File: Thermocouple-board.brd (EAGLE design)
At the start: 76.2 x 76.2 mm, 78 parts, among them J1 RJ45, J11 1X2-3.5MM, J12 1X2-3.5MM, J13 1X2-3.5MM, J14 1X2-3.5MM, J2 RJ45, J3 1981584-1, J4 2.1MMJACKTHM, J5 ST-LINK, J6 HEADER-1X3, J7 HEADER-1X2, SW1 PUSHBUTTON, SW2 PUSHBUTTON, U1 STM32F042K4, U10 MAX31855, U11 MAX31855, U12 MAX31855, U13 MAX31855, U20 EEPROM-I2C, U21 EEPROM-I2C, U30 ST3485, U31 ST3485, U40 LP298XS, X1 NX3225GD

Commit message: WIP on larger MTG holes
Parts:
- added MH1, MH2, MH3, MH4: 4-40, Thermocouple-board:MTG_HOLE_C280_H125
- added U$3, U$6: MOUNTINGHOLE2.0, microbuilder:MOUNTINGHOLE_2.0_PLATED
- moved J1 3.30 mm to (7.62, 62.7)
- moved J2 3.30 mm to (68.6, 62.7)
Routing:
- net GND: track 588.2 -> 596.4 mm
- net POE_PWR: track 58.5 -> 66.0 mm
- net UP_LINK_B: track 45.4 -> 52.0 mm
- net UP_LINK_A: track 50.6 -> 57.2 mm
- net DN_LINK_B: track 45.1 -> 51.7 mm
- net DN_LINK_A: track 50.2 -> 56.8 mm
- net +3V3: track 393.2 -> 394.7 mm

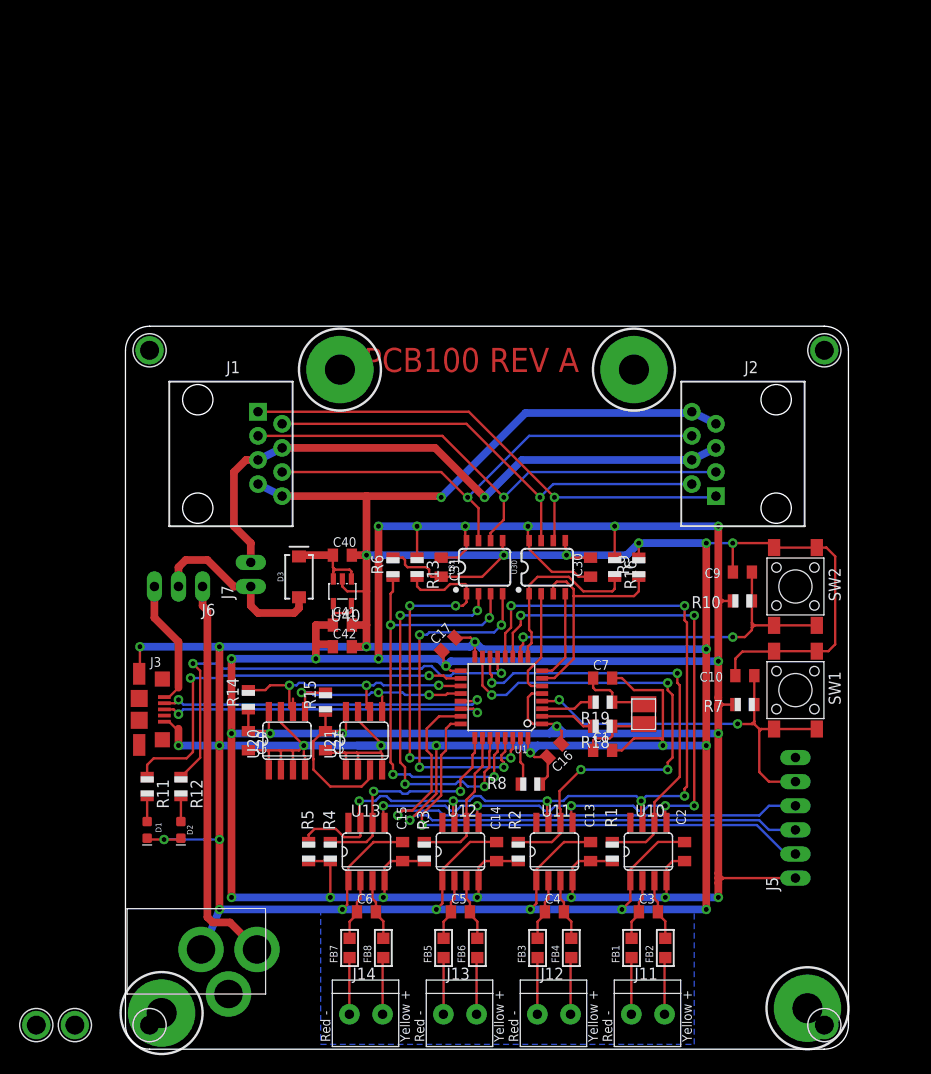
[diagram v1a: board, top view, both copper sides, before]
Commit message: Reconfigured UARTs for FTDI cable
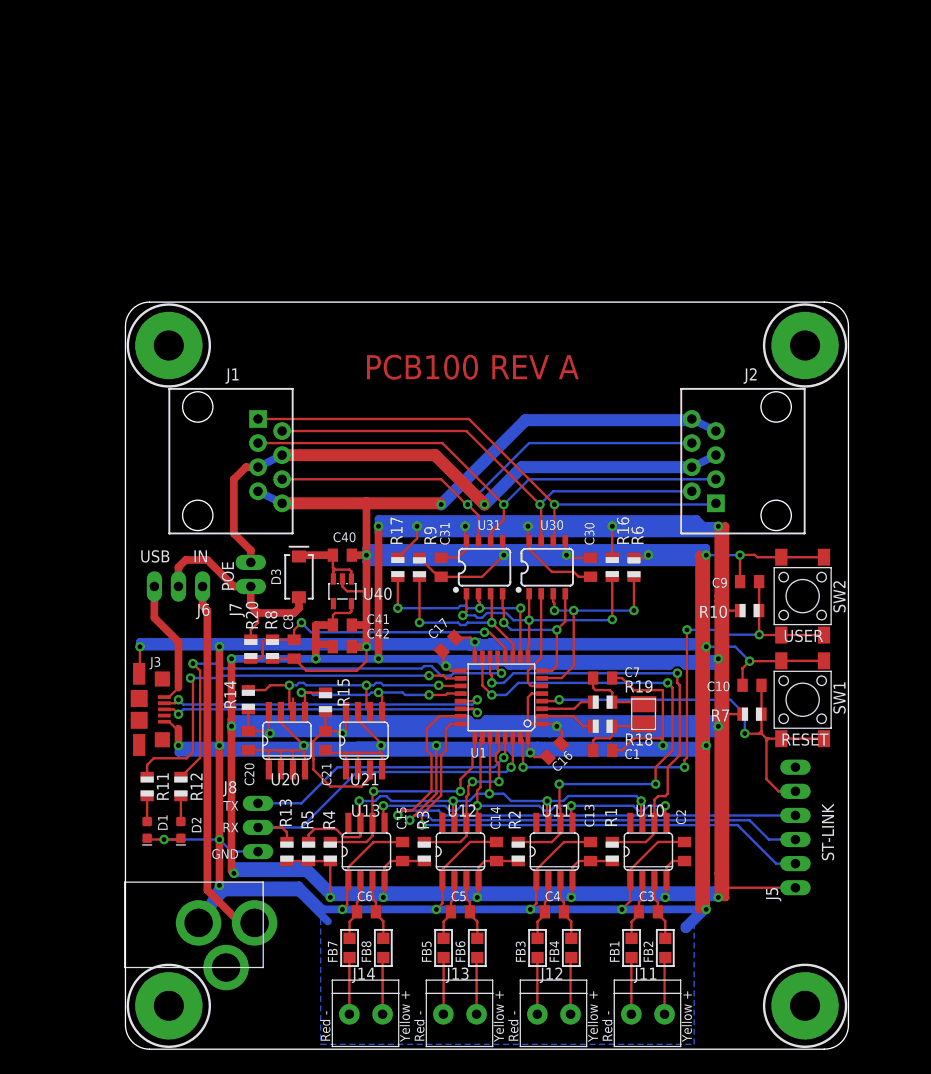
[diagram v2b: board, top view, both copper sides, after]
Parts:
- removed U$1, U$2, U$3, U$4, U$5, U$6: MOUNTINGHOLE2.0, microbuilder:MOUNTINGHOLE_2.0_PLATED
- added C8: 0.1uF, adafruit:C0805K
- added J8: HEADER-1X3, Thermocouple-board:1X03_OVAL
- added R17, R20: 10K, adafruit:R0805
- moved MH2 83.1 mm to (71.6, 4.57)
- moved MH4 69.9 mm to (71.6, 74.2)
- moved MH3 49.1 mm to (4.57, 74.2)
- moved R13 33.0 mm to (17.0, 20.8), turned to 90 degrees
- moved R8 30.7 mm to (15.5, 42.2), turned to 270 degrees
- moved R6 25.4 mm to (53.6, 50.8)
- moved R9 23.1 mm to (31.0, 50.8)
- moved J4 2.81 mm to (4.32, 13.2)
- moved R7 1.27 mm to (66.0, 35.3)
- moved C10 1.27 mm to (66.0, 38.4)
- moved C9 1.27 mm to (65.8, 49.3)
- moved R10 1.27 mm to (65.8, 46.2)
- moved SW1 1.27 mm to (71.4, 36.8)
- moved SW2 1.27 mm to (71.4, 47.8)
- moved MH1 1.08 mm to (4.57, 4.57)
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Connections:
- net +5V renamed N$21
- net UART2_RE_N renamed UART2_RE1_N
- removed net BOOT0: R8.1, U1.31
- removed net UART1_DE: R6.1, U1.28, U31.3
- removed net UART1_RE_N: U1.27, U31.2
- removed net UART2_DE: R9.1, U1.7, U30.3
- new net PWR_SENSE: C8.1, R20.2, R8.1, U1.12
- new net UART2_DE1: R6.1, U1.7, U30.3
- new net UART2_DE2: R9.1, U1.11, U31.3
- new net UART2_RE2_N: R17.2, U1.10, U31.2
- net +3V3: now also R17.1
- net BTN_USER: now also U1.31; no longer U1.10
- net GND: now also C8.2, J8.3
- net PWR: now also R20.1
- net SPI_CS2_N: now also U1.28; no longer U1.26
- net SPI_MISO: now also U1.27; no longer U1.12
- net SPI_SCK: now also U1.26; no longer U1.11
- net UART1_RX: now also J8.2; no longer U31.1
- net UART1_TX: now also J8.1; no longer U31.4
- net UART2_RX: now also U31.1
- net UART2_TX: now also U31.4
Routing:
- net +3V3: track 394.7 -> 699.6 mm
- net GND: track 596.4 -> 851.0 mm, vias 29 -> 30
- net UART1_DE: track 49.4 -> 0.00 mm, vias 4 -> 0
- net SPI_MISO: track 97.7 -> 54.9 mm, vias 7 -> 5
- net UART1_RE_N: track 42.2 -> 0.00 mm, vias 4 -> 0
- net SPI_SCK: track 84.3 -> 45.6 mm, vias 7 -> 4
- net PWR_SENSE: track 0.00 -> 31.9 mm, vias 0 -> 2
- net UART2_DE: track 23.7 -> 0.00 mm
- net UART2_DE1: track 0.00 -> 23.5 mm, vias 0 -> 3
- net UART2_RE2_N: track 0.00 -> 23.2 mm, vias 0 -> 3
- net UART2_DE2: track 0.00 -> 20.3 mm, vias 0 -> 2
- net BTN_USER: track 40.0 -> 56.0 mm, vias 2 -> 4
- net UART2_RX: track 19.2 -> 30.3 mm, vias 0 -> 3
- net UART2_TX: track 9.74 -> 18.7 mm, vias 0 -> 2
- net UART1_TX: track 38.6 -> 30.0 mm, vias 4 -> 1
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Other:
- board size 76.2 x 76.2 mm -> 76.2 x 78.7 mm
- board text added: "GND"
- board text added: "IN"
- board text added: "POE"
- board text added: "RESET"
- board text added: "RX"
- board text added: "ST-LINK"
- board text added: "TX"
- board text added: "USB"
- board text added: "USER"

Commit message: Finish routing.
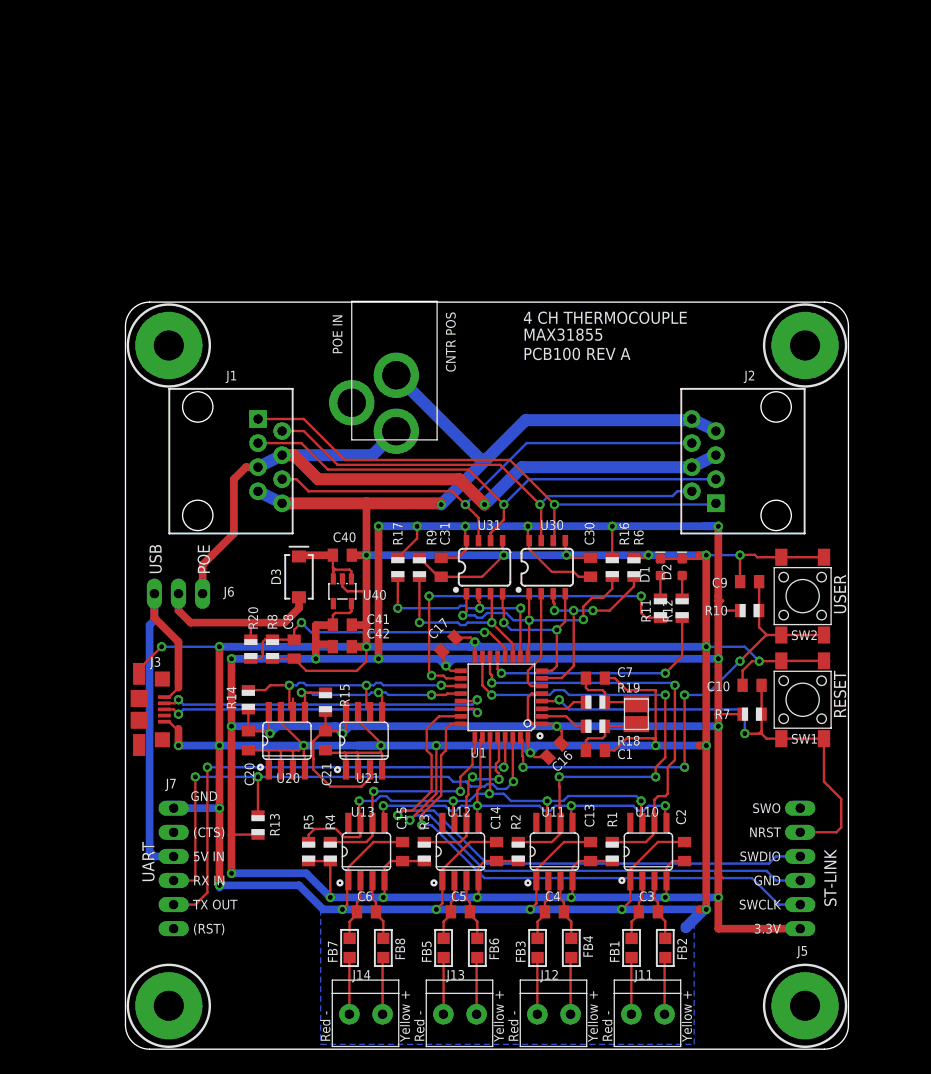
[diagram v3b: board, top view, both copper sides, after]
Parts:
- removed J8: HEADER-1X3, Thermocouple-board:1X03_OVAL
- J7: value HEADER-1X2 -> (none); device Thermocouple-board:1X02_OVAL -> Thermocouple-board:1X06_OVAL
- moved J4 65.8 mm to (28.4, 74.4), turned to 0 degrees
- moved D1 60.8 mm to (56.4, 50.8), turned to 90 degrees
- moved D2 59.6 mm to (58.7, 50.8), turned to 90 degrees
- moved R11 57.3 mm to (56.4, 46.5), turned to 90 degrees
- moved R12 56.1 mm to (58.7, 46.5), turned to 90 degrees
- moved J7 32.0 mm to (5.08, 19.1), turned to 270 degrees
- moved J5 4.35 mm to (71.1, 19.1)
- moved R13 4.13 mm to (14.0, 23.6)
- moved C1 0.76 mm to (49.5, 31.5)
- moved C7 0.76 mm to (49.5, 39.1)
- moved J6 0.76 mm to (5.59, 48.0)
- moved R18 0.76 mm to (49.5, 34.0)
- moved R19 0.76 mm to (49.5, 36.6)
- moved X1 0.76 mm to (53.8, 35.3)
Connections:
- removed net PWR_IN: J4.TIP, J6.1
- net GND: now also J7.1; no longer J8.3
- net POE_PWR: now also J4.TIP, J6.1; no longer J7.2
- net PWR: no longer J7.1
- net UART1_RX: now also J7.4; no longer J8.2
- net UART1_TX: now also J7.5; no longer J8.1
- net USB_VBUS: now also J7.3
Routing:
- net +3V3: track 699.6 -> 403.9 mm
- net GND: track 851.0 -> 609.7 mm, vias 30 -> 29
- net PWR_IN: track 38.6 -> 0.00 mm
- net USB_VBUS: track 13.6 -> 43.0 mm
- net LED_RED: track 48.4 -> 25.8 mm
- net UART1_TX: track 30.0 -> 51.7 mm, vias 1 -> 2
- net UART1_RX: track 36.7 -> 56.5 mm, vias 1 -> 3
- net POE_PWR: track 65.2 -> 82.2 mm
- net NRST: track 46.3 -> 52.8 mm
- net LED_GRN: track 43.4 -> 38.1 mm, vias 2 -> 3
- net BTN_USER: track 56.0 -> 51.1 mm
- net PWR: track 23.0 -> 18.6 mm
- net SWDIO: track 57.9 -> 60.8 mm
- net SWCLK: track 54.0 -> 56.3 mm
- net SPI_CS0_N: track 46.4 -> 44.2 mm
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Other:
- board text added: "(CTS)"
- board text added: "(RST)"
- board text added: "3.3V"
- board text added: "4 CH THERMOCOUPLE"
- board text added: "5V IN"
- board text added: "CNTR POS"
- board text added: "MAX31855"
- board text added: "NRST"
- board text added: "POE IN"
- board text added: "RX IN"
- board text added: "SWCLK"
- board text added: "SWDIO"
- board text added: "SWO"
- board text added: "TX OUT"
- board text added: "UART"
- board text removed: "IN"
- board text removed: "RX"
- board text removed: "TX"

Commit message: Finish cleanup. Added schem frame.
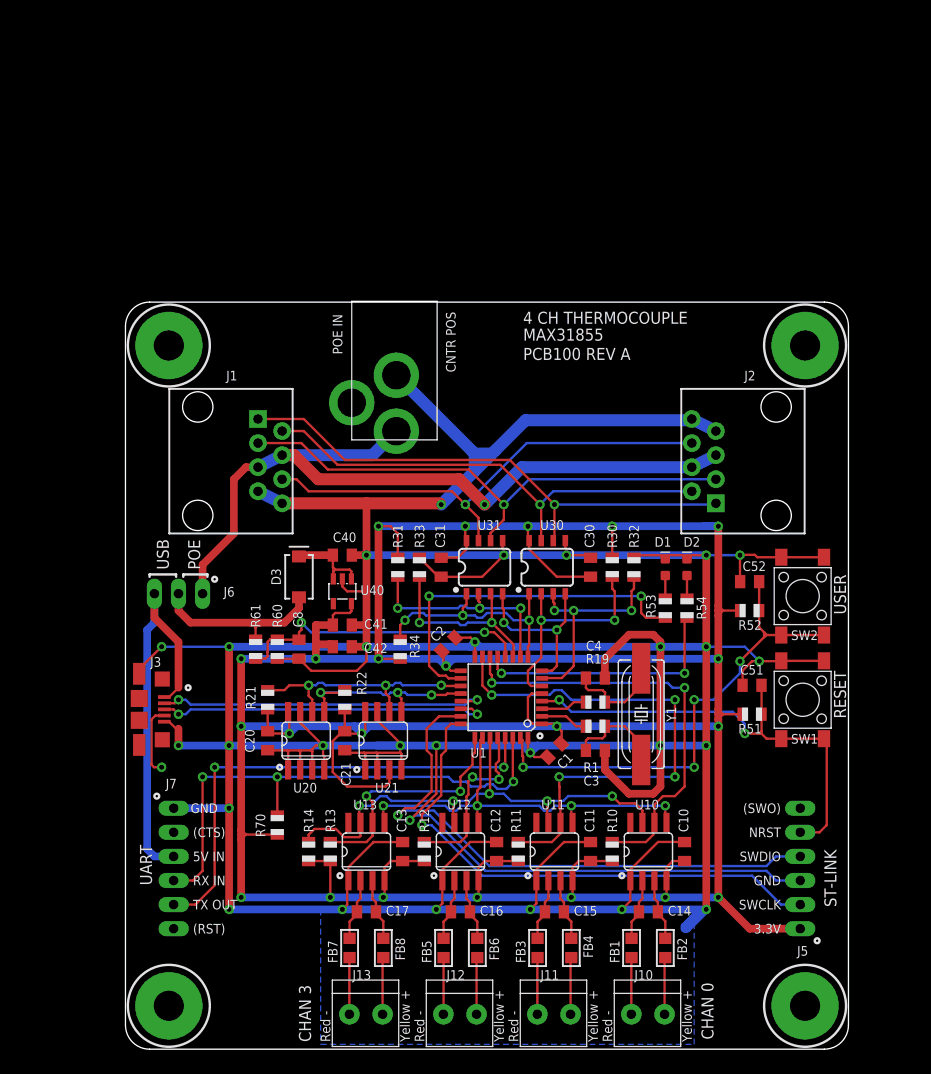
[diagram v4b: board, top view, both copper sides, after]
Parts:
- removed C5, C6: 0.01uF, adafruit:C0805K
- removed C7: 0.1uF, adafruit:C0805K
- removed J14: 1X2-3.5MM, Thermocouple-board:1X2-3.5MM
- removed R15, R18, R2, R20, R3, R4, R5, R8: 10K, adafruit:R0805
- removed X1: NX3225GD, Thermocouple-board:NX3225-2P
- added C11, C12, C51: 0.1uF, adafruit:C0805K
- added J10: 1X2-3.5MM, Thermocouple-board:1X2-3.5MM
- added R21, R22, R34, R52, R60, R61, R70: 10K, adafruit:R0805
- added R53, R54: 470, adafruit:R0805
- added Y1: 8MHz, SparkFun-Clocks:HC49UP
- C14, C15, C16, C17: value 0.1uF -> 0.01uF
- C3, C4: value 0.01uF -> 10pF
- J7: value (none) -> UART
- R11, R12: value 470 -> 10K
- moved R12 37.4 mm to (31.5, 20.8)
- moved C2 33.1 mm to (34.0, 42.7), turned to 45 degrees
- moved R11 29.7 mm to (41.4, 20.8)
- moved C17 29.5 mm to (25.4, 14.5), turned to 0 degrees
- moved R10 29.2 mm to (51.3, 20.8), turned to 90 degrees
- moved C4 25.0 mm to (49.5, 39.1)
- moved C13 19.8 mm to (29.2, 20.8)
- moved C16 19.7 mm to (35.3, 14.5), turned to 0 degrees
- moved C10 18.9 mm to (58.9, 20.8), turned to 90 degrees
- moved C3 17.9 mm to (49.5, 31.5)
- moved C14 17.2 mm to (55.1, 14.5), turned to 0 degrees
- moved C15 17.2 mm to (45.2, 14.5), turned to 0 degrees
- moved R14 17.2 mm to (19.3, 20.8)
- moved R1 13.3 mm to (49.5, 34.0), turned to 180 degrees
- moved J12 9.91 mm to (35.3, 3.68)
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- renumbered C9 to C52, R16 to R30, R17 to R31, R6 to R32, R7 to R51, R9 to R33
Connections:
- removed net PWR: D3.A, J6.2, R20.1
- new net PWR_IN: D3.A, J6.2, R61.1
- new net USB_ID: J3.4
- net +3V3: now also C1.1, C10.1, C11.1, C12.1, R11.1, R12.1, R21.1, R22.1, R34.1, R52.1, R70.1; no longer C14.1, C15.1, C16.1, C17.1, R1.1, R15.1, R2.1, R3.1, R4.1, R5.1
- net BTN_USER: now also R52.2; no longer R10.2
- net GND: now also C11.2, C12.2, C3.2, C4.2, C51.2, R60.2; no longer C14.2, C15.2, C16.2, C17.2, C7.2, R8.2
- net I2C_SCL: now also R21.2; no longer R14.2
- net I2C_SDA: now also R22.2; no longer R15.2
- net LED_GRN: now also R53.1; no longer R11.1
- net LED_RED: now also R54.1; no longer R12.1
- net N$1: now also J10.1; no longer J11.1
- net N$10: now also C15.2; no longer C4.2
- net N$11: now also J12.1; no longer J13.1
- net N$12: now also C16.1; no longer C5.1
- net N$13: now also J12.2; no longer J13.2
- net N$14: now also C16.2; no longer C5.2
- net N$15: now also J13.1; no longer J14.1
- net N$16: now also C17.1; no longer C6.1
- net N$17: now also J13.2; no longer J14.2
- net N$18: now also C17.2; no longer C6.2
- net N$19: now also C4.1, Y1.2; no longer C7.1, X1.2
- net N$2: now also R1.2; no longer R18.2
- net N$20: now also C3.1, R1.1, Y1.1; no longer C1.1, R18.1, X1.1
- net N$25: now also R53.2; no longer R11.2
- net N$26: now also R54.2; no longer R12.2
- net N$4: now also C14.1; no longer C3.1
- net N$5: now also J10.2; no longer J11.2
- net N$6: now also C14.2; no longer C3.2
- net N$7: now also J11.1; no longer J12.1
- net N$8: now also C15.1; no longer C4.1
- net N$9: now also J11.2; no longer J12.2
- net NRST: now also C51.1; no longer C10.1
- net PWR_SENSE: now also R60.1, R61.2; no longer R20.2, R8.1
- net SPI_CS0_N: now also R10.2; no longer R1.2
- net SPI_CS1_N: now also R11.2; no longer R2.2
- net SPI_CS2_N: now also R12.2; no longer R3.2
- net SPI_CS3_N: now also R13.2; no longer R4.2
- net SPI_MISO: now also R14.2; no longer R5.2
- net UART1_RX: now also R70.2; no longer R13.2
- net UART2_RE1_N: now also R30.2
- net UART2_RX: now also R34.2; no longer R30.2
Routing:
- net GND: track 609.7 -> 630.1 mm
- net PWR_IN: track 0.00 -> 20.0 mm
- net PWR: track 18.6 -> 0.00 mm
- net UART2_RE1_N: track 11.6 -> 24.0 mm, vias 0 -> 2
- net USB_ID: track 0.00 -> 7.46 mm, vias 0 -> 1
- net +3V3: track 403.9 -> 407.6 mm, vias 23 -> 22
- net UART2_RX: track 29.2 -> 25.7 mm
- net I2C_SCL: track 30.3 -> 26.9 mm
- net N$20: track 7.68 -> 10.6 mm
- net N$19: track 7.68 -> 10.6 mm
- net NRST: track 52.8 -> 50.0 mm
- net SPI_CS1_N: track 53.3 -> 55.6 mm
- net I2C_SDA: track 24.0 -> 22.1 mm
- net SPI_CS0_N: track 44.2 -> 45.8 mm
- net LED_RED: track 25.8 -> 27.2 mm
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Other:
- board text added: "(SWO)"
- board text added: "CHAN 0"
- board text added: "CHAN 3"
- board text removed: "SWO"
